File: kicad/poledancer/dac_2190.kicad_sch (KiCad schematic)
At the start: 22 parts, among them U9 AD5328

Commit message: geo reannotate
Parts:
- renumbered C23 to C22, C22 to C25, C45 to C26, C21 to C27, C24 to C6, C20 to C7, C19 to C8, C18 to C9, R21 to R13, R25 to R14, R7 to R15, R17 to R16, R22 to R17, R19 to R48, R20 to R50, R18 to R51, R23 to R53, R6 to R54, R24 to R55, R5 to R57, U9 to U6

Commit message: v0.1 sent to manufacture
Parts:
- C10: value 22n -> 0.1u; LCSC C21122 -> C14663
- C22, C25, C27, C6, C7: value 22n -> 47n; LCSC C21122 -> C1622
- R13, R16, R48, R50, R51: LCSC C17936 -> C25804
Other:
- note added: "QCTRL input is current, abs max of 500uA with 222uA for oscillation using standard resonance setup. Target around 320uA with an RC filter @ 800 Hz"
- note added: "SSI2190 Control: Max control current 100uA. Run DAC @ 2.5V (1X scale). RC filter @ ~560 Hz"
- note removed: "QCTRL input is current, abs max of 500uA with 222uA for oscillation using standard resonance setup. Target around 320uA with an RC filter @ 927 Hz"
- note removed: "SSI2190 Control: Max control current 100uA. Run DAC @ 2.5V (1X scale). RC filter @ 600 Hz"
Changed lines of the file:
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@@
     (fill (type none))
   )
-  (text "QCTRL input is current, abs max of 500uA\nwith 222uA for oscillation using standard resonance setup.\nTarget around 320uA with an RC filter @ 927 Hz"
+  (text "QCTRL input is current, abs max of 500uA\nwith 222uA for oscillation using standard resonance setup.\nTarget around 320uA with an RC filter @ 800 Hz"
     (at 50.8 118.11 0)
     (effects (font (size 1.27 1.27)) (justify left bottom))
   )
-  (text "SSI2190 Control:\nMax control current 100uA.\nRun DAC @ 2.5V (1X scale).\nRC filter @ 600 Hz"
+  (text "SSI2190 Control:\nMax control current 100uA.\nRun DAC @ 2.5V (1X scale).\nRC filter @ ~560 Hz"
     (at 173.355 26.67 0)
     (effects (font (size 1.27 1.27)) (justify left bottom))
@@
       (effects (font (size 1.27 1.27)) hide)
     )
-    (property "LCSC" "C17936" (at 201.93 38.1 0)
+    (property "LCSC" "C25804" (at 201.93 38.1 0)
       (effects (font (size 1.27 1.27)) hide)
     )
@@
       (effects (font (size 1.27 1.27)))
     )
-    (property "Value" "22n" (at 72.39 133.985 0)
+    (property "Value" "0.1u" (at 72.39 133.985 0)
       (effects (font (size 1.27 1.27)))
     )
@@
       (effects (font (size 1.27 1.27)) hide)
     )
-    (property "LCSC" "C21122" (at 76.835 131.445 0)
+    (property "LCSC" "C14663" (at 76.835 131.445 0)
       (effects (font (size 1.27 1.27)) hide)
     )
@@
       (effects (font (size 1.27 1.27)))
     )
-    (property "Value" "22n" (at 206.375 92.075 0)
+    (property "Value" "47n" (at 206.375 92.075 0)
       (effects (font (size 1.27 1.27)))
     )
@@
       (effects (font (size 1.27 1.27)) hide)
     )
-    (property "LCSC" "C21122" (at 210.82 89.535 0)
+    (property "LCSC" "C1622" (at 210.82 89.535 0)
       (effects (font (size 1.27 1.27)) hide)
     )
@@
       (effects (font (size 1.27 1.27)))
     )
-    (property "Value" "22n" (at 206.375 140.97 0)
+    (property "Value" "47n" (at 206.375 140.97 0)
       (effects (font (size 1.27 1.27)))
     )
@@
       (effects (font (size 1.27 1.27)) hide)
     )
-    (property "LCSC" "C21122" (at 210.82 138.43 0)
+    (property "LCSC" "C1622" (at 210.82 138.43 0)
       (effects (font (size 1.27 1.27)) hide)
     )
@@
       (effects (font (size 1.27 1.27)) hide)
     )
-    (property "LCSC" "C17936" (at 201.93 60.96 0)
+    (property "LCSC" "C25804" (at 201.93 60.96 0)
       (effects (font (size 1.27 1.27)) hide)
     )
@@
       (effects (font (size 1.27 1.27)) hide)
     )
-    (property "LCSC" "C17936" (at 201.93 107.95 0)
+    (property "LCSC" "C25804" (at 201.93 107.95 0)
       (effects (font (size 1.27 1.27)) hide)
     )
@@
       (effects (font (size 1.27 1.27)))
     )
-    (property "Value" "22n" (at 206.375 45.72 0)
+    (property "Value" "47n" (at 206.375 45.72 0)
       (effects (font (size 1.27 1.27)))
     )
@@
       (effects (font (size 1.27 1.27)) hide)
     )
-    (property "LCSC" "C21122" (at 210.82 43.18 0)
+    (property "LCSC" "C1622" (at 210.82 43.18 0)
       (effects (font (size 1.27 1.27)) hide)
     )
@@
       (effects (font (size 1.27 1.27)) hide)
     )
-    (property "LCSC" "C17936" (at 201.93 133.35 0)
+    (property "LCSC" "C25804" (at 201.93 133.35 0)
       (effects (font (size 1.27 1.27)) hide)
     )
@@
       (effects (font (size 1.27 1.27)))
     )
-    (property "Value" "22n" (at 206.375 68.58 0)
+    (property "Value" "47n" (at 206.375 68.58 0)
       (effects (font (size 1.27 1.27)))
     )
@@
       (effects (font (size 1.27 1.27)) hide)
     )
-    (property "LCSC" "C21122" (at 210.82 66.04 0)
+    (property "LCSC" "C1622" (at 210.82 66.04 0)
       (effects (font (size 1.27 1.27)) hide)
     )
@@
       (effects (font (size 1.27 1.27)))
     )
-    (property "Value" "22n" (at 206.375 115.57 0)
+    (property "Value" "47n" (at 206.375 115.57 0)
       (effects (font (size 1.27 1.27)))
     )
@@
       (effects (font (size 1.27 1.27)) hide)
     )
-    (property "LCSC" "C21122" (at 210.82 113.03 0)
+    (property "LCSC" "C1622" (at 210.82 113.03 0)
       (effects (font (size 1.27 1.27)) hide)
     )
@@
       (effects (font (size 1.27 1.27)) hide)
     )
-    (property "LCSC" "C17936" (at 201.93 84.455 0)
-      (effects (font (size 1.27 1.27)) hide)
-    )
+    (property "LCSC" "C25804" (at 201.93 84.455 0)
+      (effects (font (size 1.27 1.27)) hide)
+    )

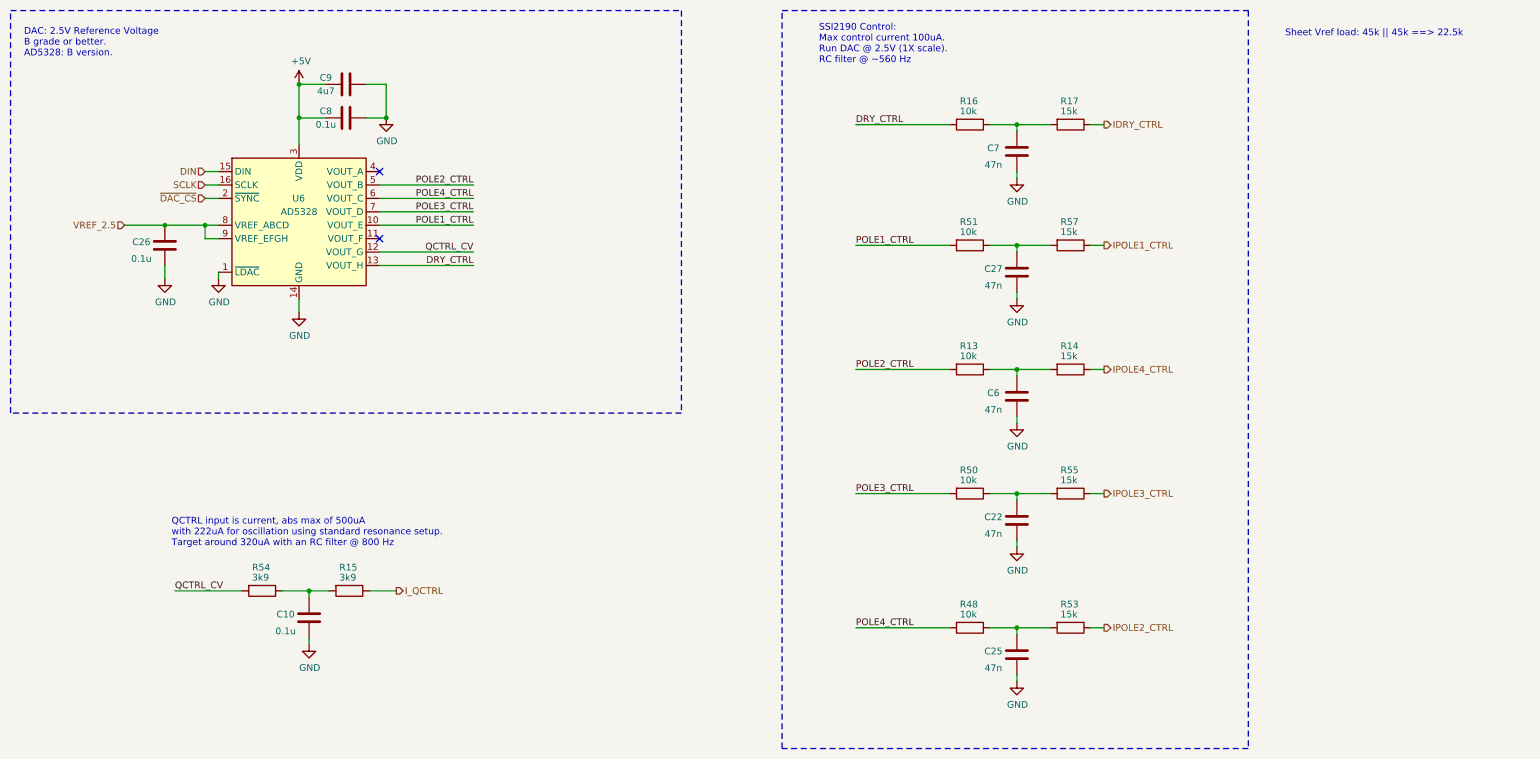
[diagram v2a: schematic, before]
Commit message: fix label error between pole2/pole4 in DAC channels in schematic.  no layout change.
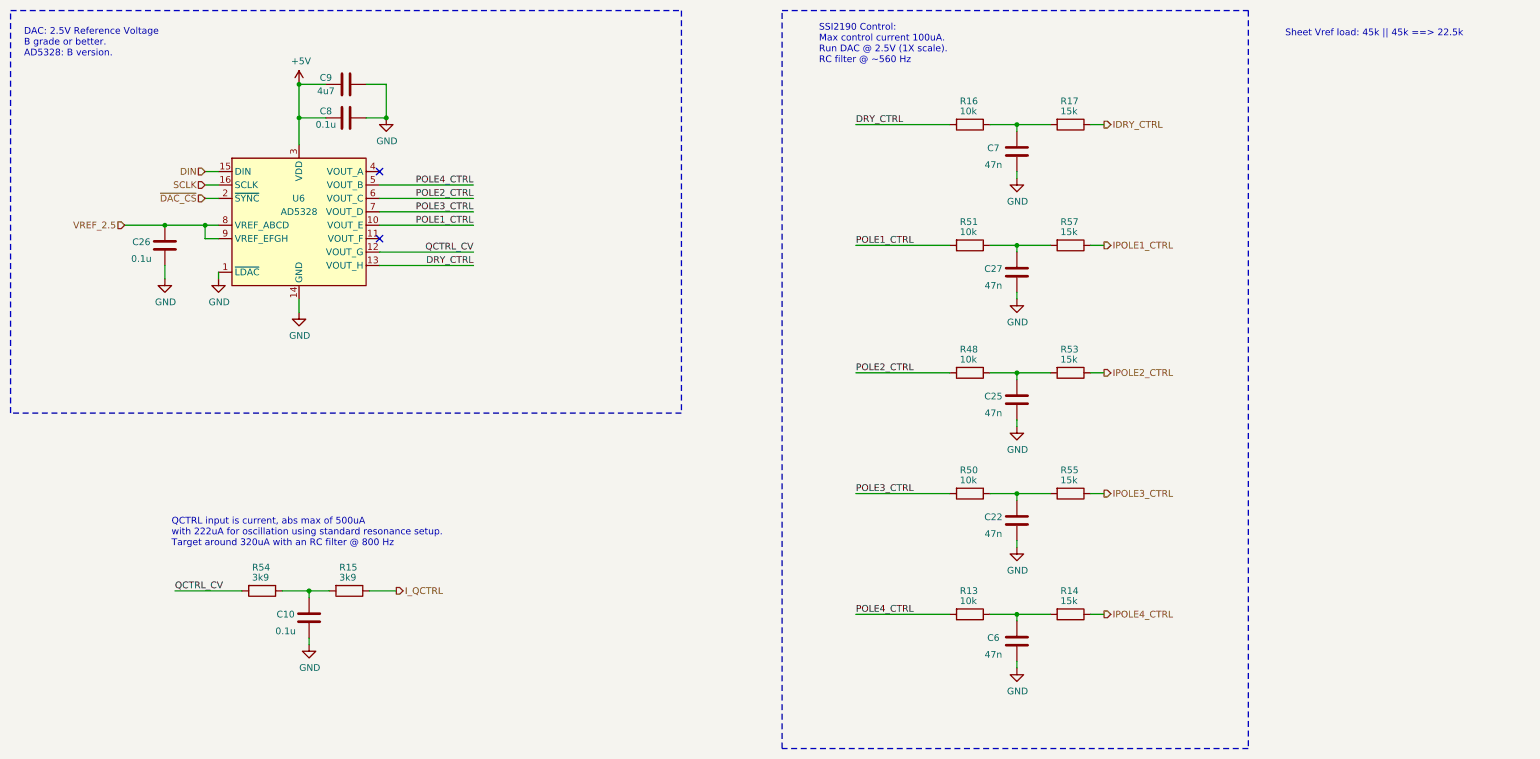
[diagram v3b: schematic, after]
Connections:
- net POLE2_CTRL: now also R48.2, U6.6 (VOUT_C); no longer R13.2, U6.5 (VOUT_B)
- net POLE4_CTRL: now also R13.2, U6.5 (VOUT_B); no longer R48.2, U6.6 (VOUT_C)
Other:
- moved on the sheet: C25, C6, R13, R14, R48, R53

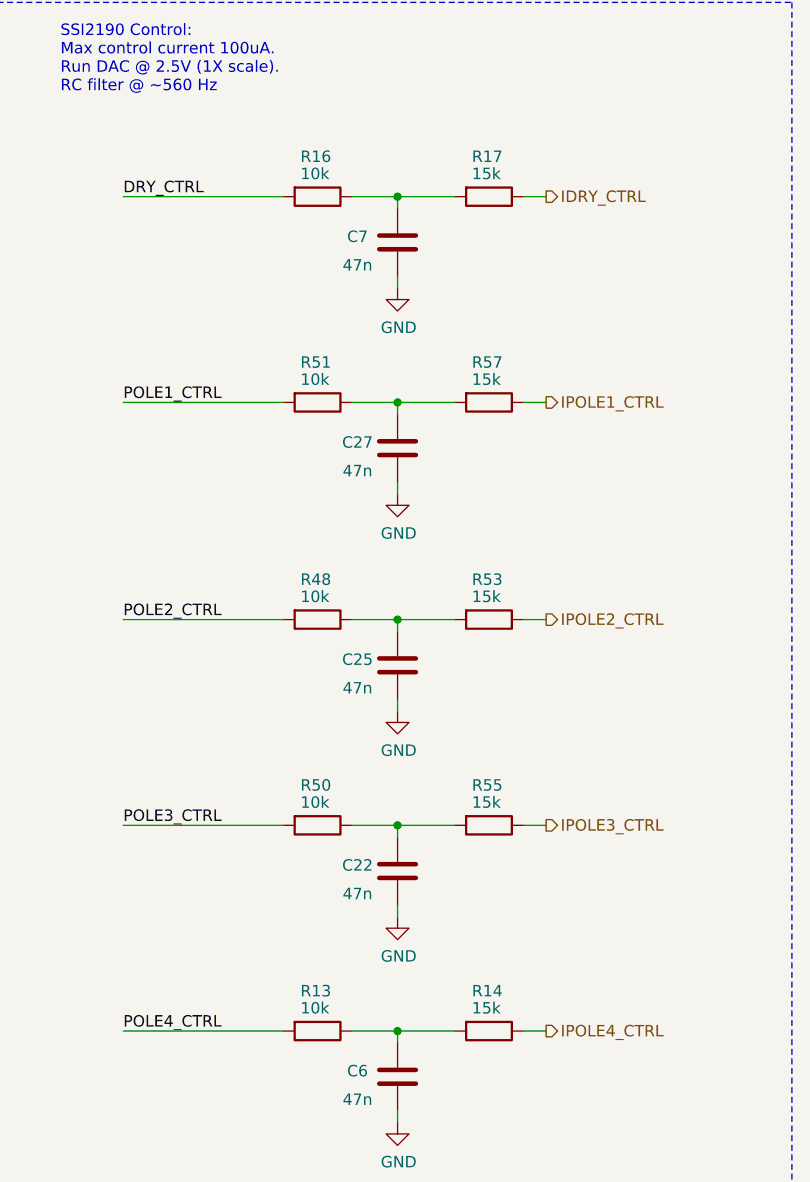
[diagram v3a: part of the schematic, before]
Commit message: changed linear mod amount for z3340, from tame to wild now.  Updated poledancer 2140, better DAC RC filter (higher freq) for 2190.
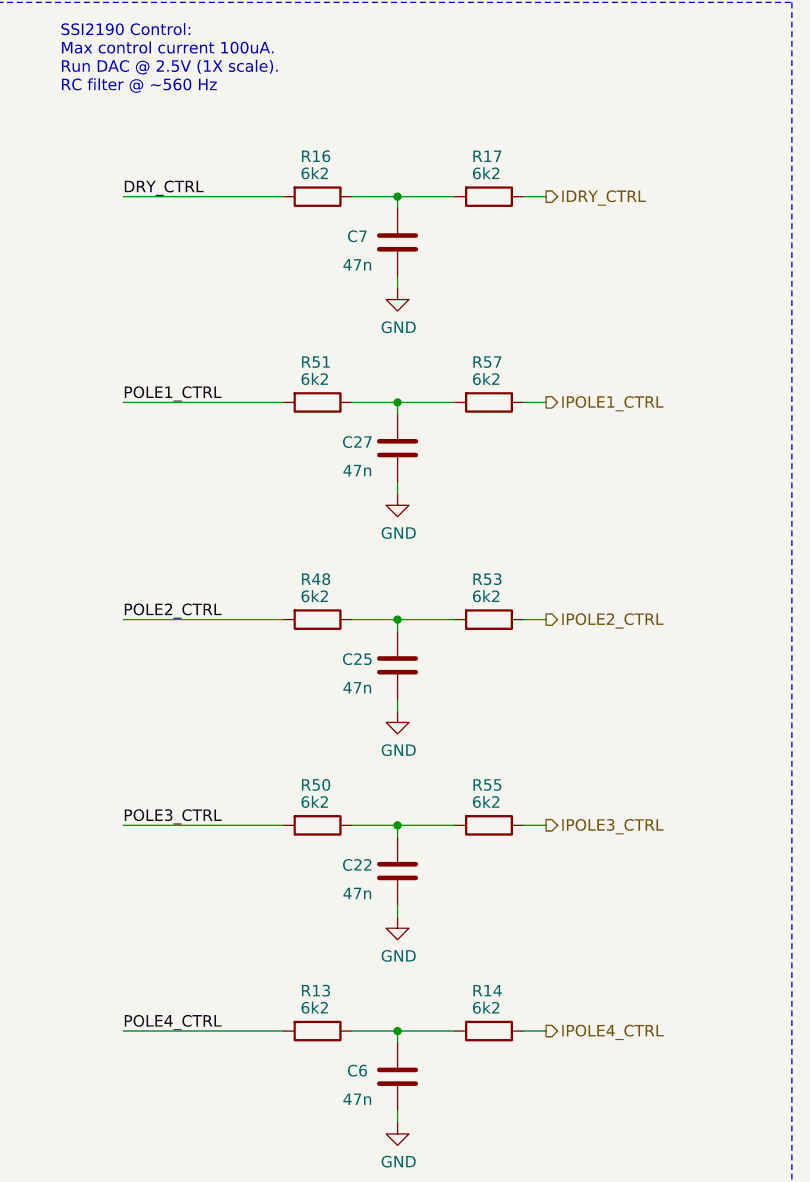
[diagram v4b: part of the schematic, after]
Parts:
- R13, R16, R48, R50, R51: value 10k -> 6k2; LCSC C25804 -> C4260
- R14, R17, R53, R55, R57: value 15k -> 6k2; LCSC C22809 -> C4260
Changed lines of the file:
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@@
       (effects (font (size 1.27 1.27)) (justify left))
     )
-    (property "Value" "15k" (at 219.075 128.27 90)
+    (property "Value" "6k2" (at 219.075 128.27 90)
       (effects (font (size 1.27 1.27)) (justify left))
     )
@@
       (effects (font (size 1.27 1.27)) hide)
     )
-    (property "LCSC" "C22809" (at 220.98 130.81 0)
+    (property "LCSC" "C4260" (at 220.98 130.81 0)
       (effects (font (size 1.27 1.27)) hide)
     )
@@
       (effects (font (size 1.27 1.27)) (justify left))
     )
-    (property "Value" "15k" (at 219.075 105.41 90)
+    (property "Value" "6k2" (at 219.075 105.41 90)
       (effects (font (size 1.27 1.27)) (justify left))
     )
@@
       (effects (font (size 1.27 1.27)) hide)
     )
-    (property "LCSC" "C22809" (at 220.98 107.95 0)
+    (property "LCSC" "C4260" (at 220.98 107.95 0)
       (effects (font (size 1.27 1.27)) hide)
     )
@@
       (effects (font (size 1.27 1.27)) (justify left))
     )
-    (property "Value" "15k" (at 219.075 82.55 90)
+    (property "Value" "6k2" (at 219.075 82.55 90)
       (effects (font (size 1.27 1.27)) (justify left))
     )
@@
       (effects (font (size 1.27 1.27)) hide)
     )
-    (property "LCSC" "C22809" (at 220.98 85.09 0)
+    (property "LCSC" "C4260" (at 220.98 85.09 0)
       (effects (font (size 1.27 1.27)) hide)
     )
@@
       (effects (font (size 1.27 1.27)) (justify left))
     )
-    (property "Value" "10k" (at 200.025 35.56 90)
+    (property "Value" "6k2" (at 200.025 35.56 90)
       (effects (font (size 1.27 1.27)) (justify left))
     )
@@
       (effects (font (size 1.27 1.27)) hide)
     )
-    (property "LCSC" "C25804" (at 201.93 38.1 0)
+    (property "LCSC" "C4260" (at 201.93 38.1 0)
       (effects (font (size 1.27 1.27)) hide)
     )
@@
       (effects (font (size 1.27 1.27)) (justify left))
     )
-    (property "Value" "15k" (at 219.075 58.42 90)
+    (property "Value" "6k2" (at 219.075 58.42 90)
       (effects (font (size 1.27 1.27)) (justify left))
     )
@@
       (effects (font (size 1.27 1.27)) hide)
     )
-    (property "LCSC" "C22809" (at 220.98 60.96 0)
+    (property "LCSC" "C4260" (at 220.98 60.96 0)
       (effects (font (size 1.27 1.27)) hide)
     )
@@
       (effects (font (size 1.27 1.27)) (justify left))
     )
-    (property "Value" "10k" (at 200.025 58.42 90)
+    (property "Value" "6k2" (at 200.025 58.42 90)
       (effects (font (size 1.27 1.27)) (justify left))
     )
@@
       (effects (font (size 1.27 1.27)) hide)
     )
-    (property "LCSC" "C25804" (at 201.93 60.96 0)
+    (property "LCSC" "C4260" (at 201.93 60.96 0)
       (effects (font (size 1.27 1.27)) hide)
     )
@@
       (effects (font (size 1.27 1.27)) (justify left))
     )
-    (property "Value" "10k" (at 200.025 105.41 90)
+    (property "Value" "6k2" (at 200.025 105.41 90)
       (effects (font (size 1.27 1.27)) (justify left))
     )
@@
       (effects (font (size 1.27 1.27)) hide)
     )
-    (property "LCSC" "C25804" (at 201.93 107.95 0)
+    (property "LCSC" "C4260" (at 201.93 107.95 0)
       (effects (font (size 1.27 1.27)) hide)
     )
@@
       (effects (font (size 1.27 1.27)) (justify left))
     )
-    (property "Value" "15k" (at 219.075 35.56 90)
+    (property "Value" "6k2" (at 219.075 35.56 90)
       (effects (font (size 1.27 1.27)) (justify left))
     )
@@
       (effects (font (size 1.27 1.27)) hide)
     )
-    (property "LCSC" "C22809" (at 220.98 38.1 0)
+    (property "LCSC" "C4260" (at 220.98 38.1 0)
       (effects (font (size 1.27 1.27)) hide)
     )
@@
       (effects (font (size 1.27 1.27)) (justify left))
     )
-    (property "Value" "10k" (at 200.025 82.55 90)
+    (property "Value" "6k2" (at 200.025 82.55 90)
       (effects (font (size 1.27 1.27)) (justify left))
     )
@@
       (effects (font (size 1.27 1.27)) hide)
     )
-    (property "LCSC" "C25804" (at 201.93 85.09 0)
+    (property "LCSC" "C4260" (at 201.93 85.09 0)
       (effects (font (size 1.27 1.27)) hide)
     )
@@
       (effects (font (size 1.27 1.27)) (justify left))
     )
-    (property "Value" "10k" (at 200.025 128.27 90)
+    (property "Value" "6k2" (at 200.025 128.27 90)
       (effects (font (size 1.27 1.27)) (justify left))
     )
@@
       (effects (font (size 1.27 1.27)) hide)
     )
-    (property "LCSC" "C25804" (at 201.93 130.81 0)
-      (effects (font (size 1.27 1.27)) hide)
-    )
+    (property "LCSC" "C4260" (at 201.93 130.81 0)
+      (effects (font (size 1.27 1.27)) hide)
+    )
